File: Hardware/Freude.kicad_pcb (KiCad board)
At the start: 4 copper layers, 30 parts, among them J1 Conn_01x06_Female, J2 Conn_01x05_Female, J3 Conn_01x06_Female, J4 Conn_01x04_Female, J5 Conn_01x04_Female, J6 Conn_01x04_Male, U1 IQS572, U2 STM32L432KBUx, X1 Custom_Touchpad, Y1 Crystal_GND24

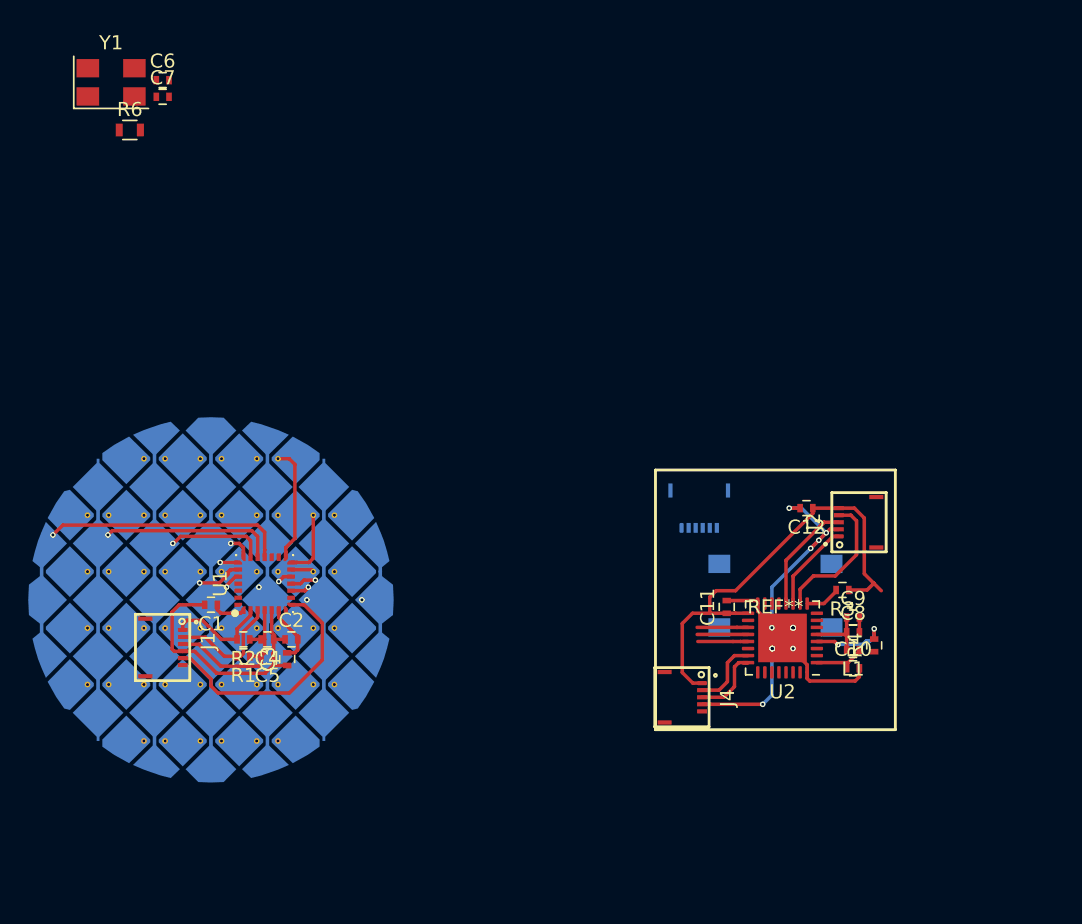
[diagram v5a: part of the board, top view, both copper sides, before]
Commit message: add detail to joystick envelope, changed sides of connectors to better fit joystick, reroute in progress
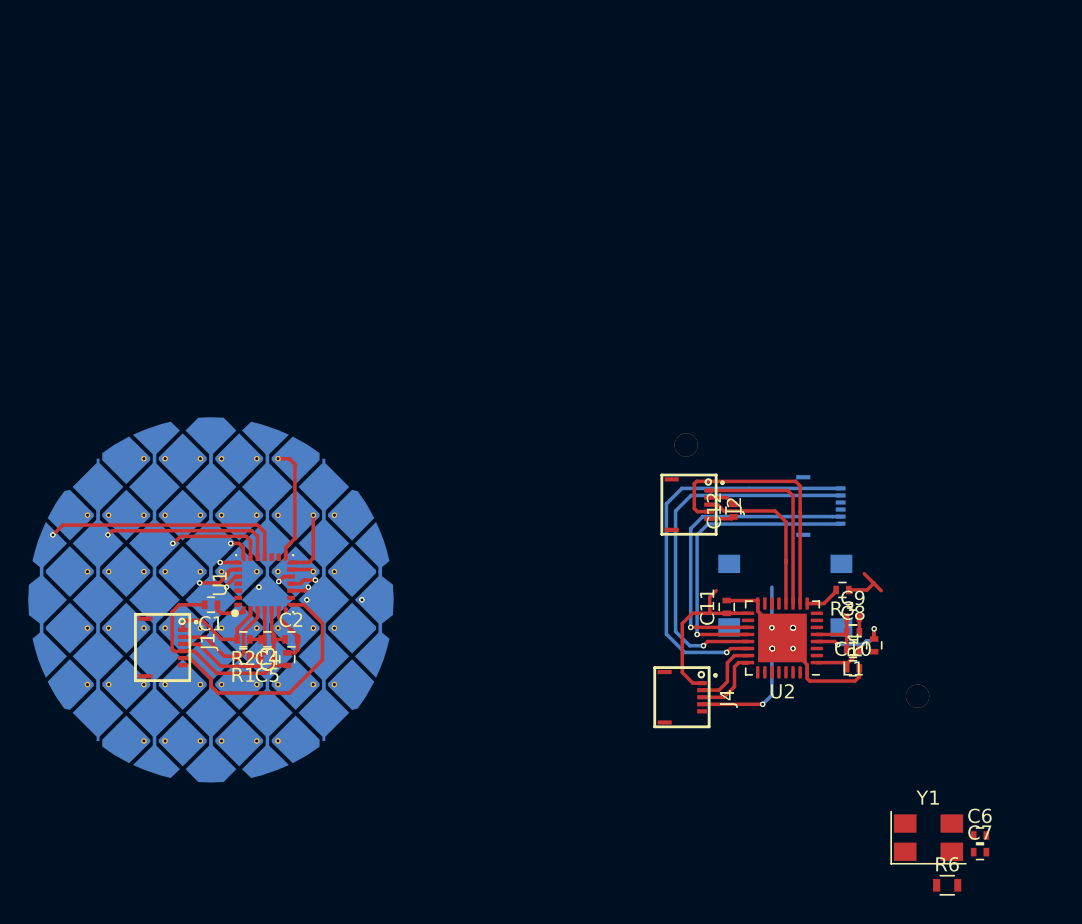
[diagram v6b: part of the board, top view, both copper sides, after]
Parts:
- REF**: moved to B.Cu
- moved C6 78.9 mm to (214.5, 96.7)
- moved C7 78.9 mm to (214.5, 97.9)
- moved R6 78.9 mm to (212.2, 100.2)
- moved Y1 78.9 mm to (210.9, 96.9)
- moved J3 10.1 mm to (204.6, 73.3), turned to 90 degrees
- moved J2 9.28 mm to (195.3, 73.2), turned to 270 degrees
- moved C12 5.18 mm to (197.0, 73.7), turned to 90 degrees
- moved REF** 0.70 mm to (200.7, 79.7)
- moved REF** 0.18 mm to (200.0, 79.8), turned to 180 degrees
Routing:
- net /AZO_UNK: track 0.00 -> 28.5 mm, vias 0 -> 1
- net /RDY_UC: track 3.56 -> 26.4 mm, vias 0 -> 1
- net /SCL_UC: track 3.61 -> 22.0 mm, vias 0 -> 1
- net /SDA_UC: track 3.61 -> 21.2 mm, vias 0 -> 1
- net +3V3: track 36.9 -> 21.3 mm
- net GND: track 39.7 -> 29.5 mm, vias 15 -> 11
- net /DAC1_OUT2: track 9.84 -> 18.9 mm
- net /DAC2_OUT1: track 6.36 -> 13.7 mm
- net /Switch_Out: track 8.43 -> 11.9 mm
